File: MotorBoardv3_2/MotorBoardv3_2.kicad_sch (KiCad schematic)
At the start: 79 parts, among them J1 Bump0, J11 GP2Y0A41SK0F, J12 GP2Y0A41SK0F, J13 GP2Y0A41SK0F, J15 7.2, J16 LP5.0, J17 ELA, J18 ERA, J19 Voltage Display, J2 Bump1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

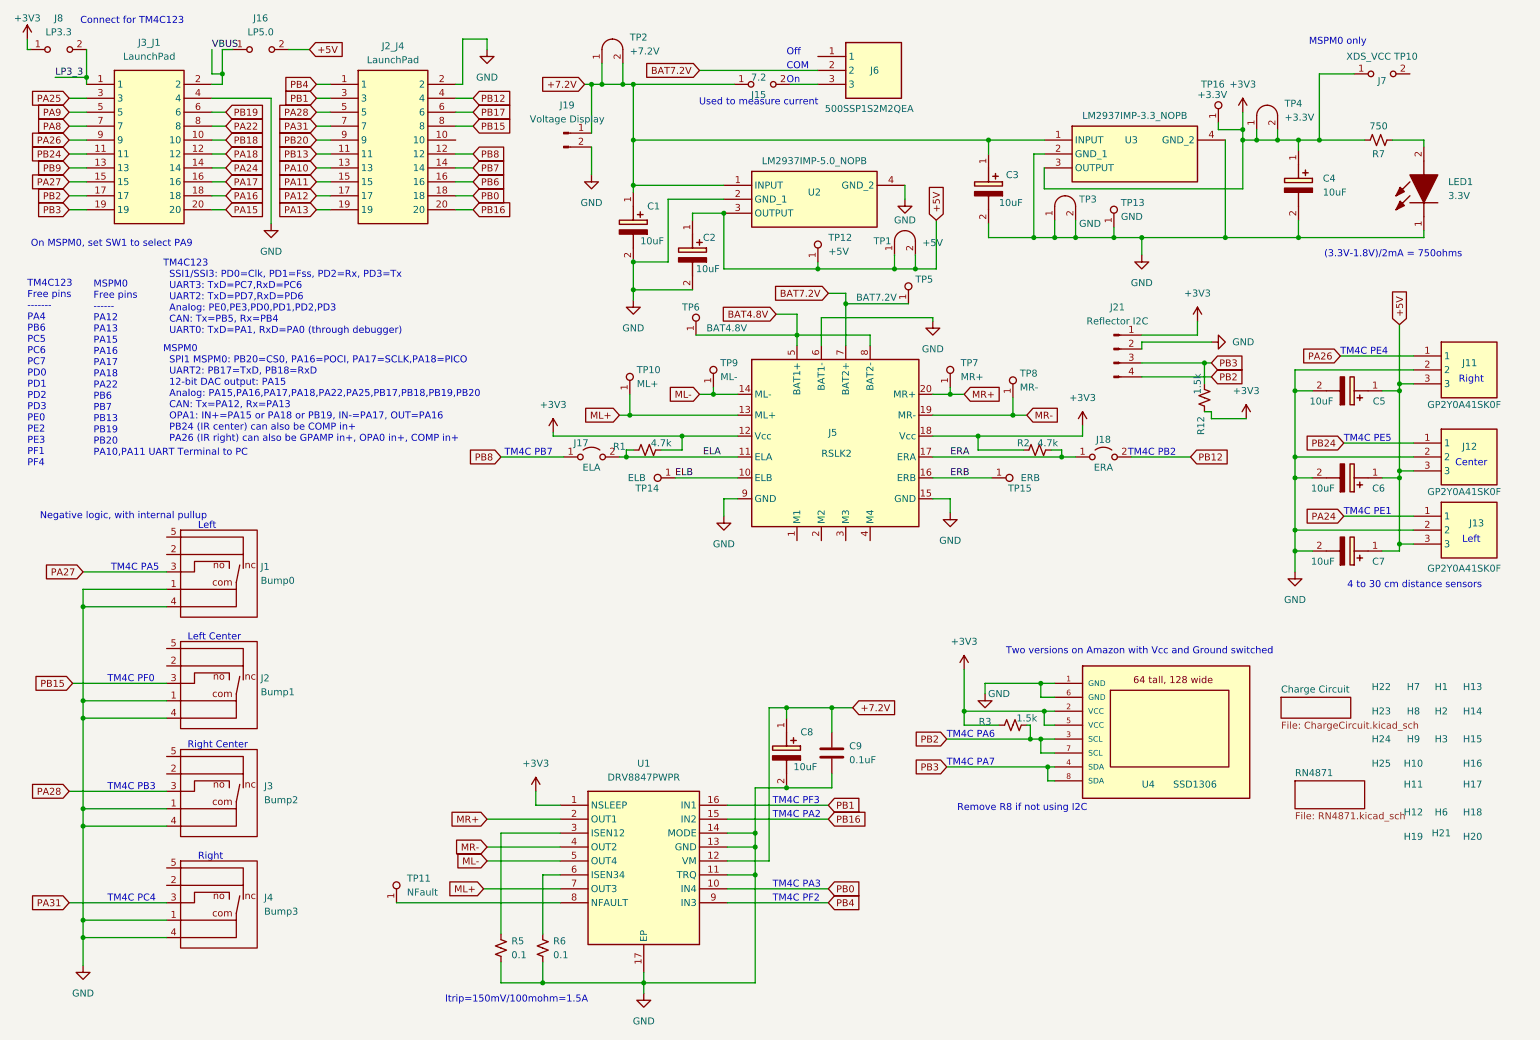
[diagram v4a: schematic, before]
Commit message: Added voltage display
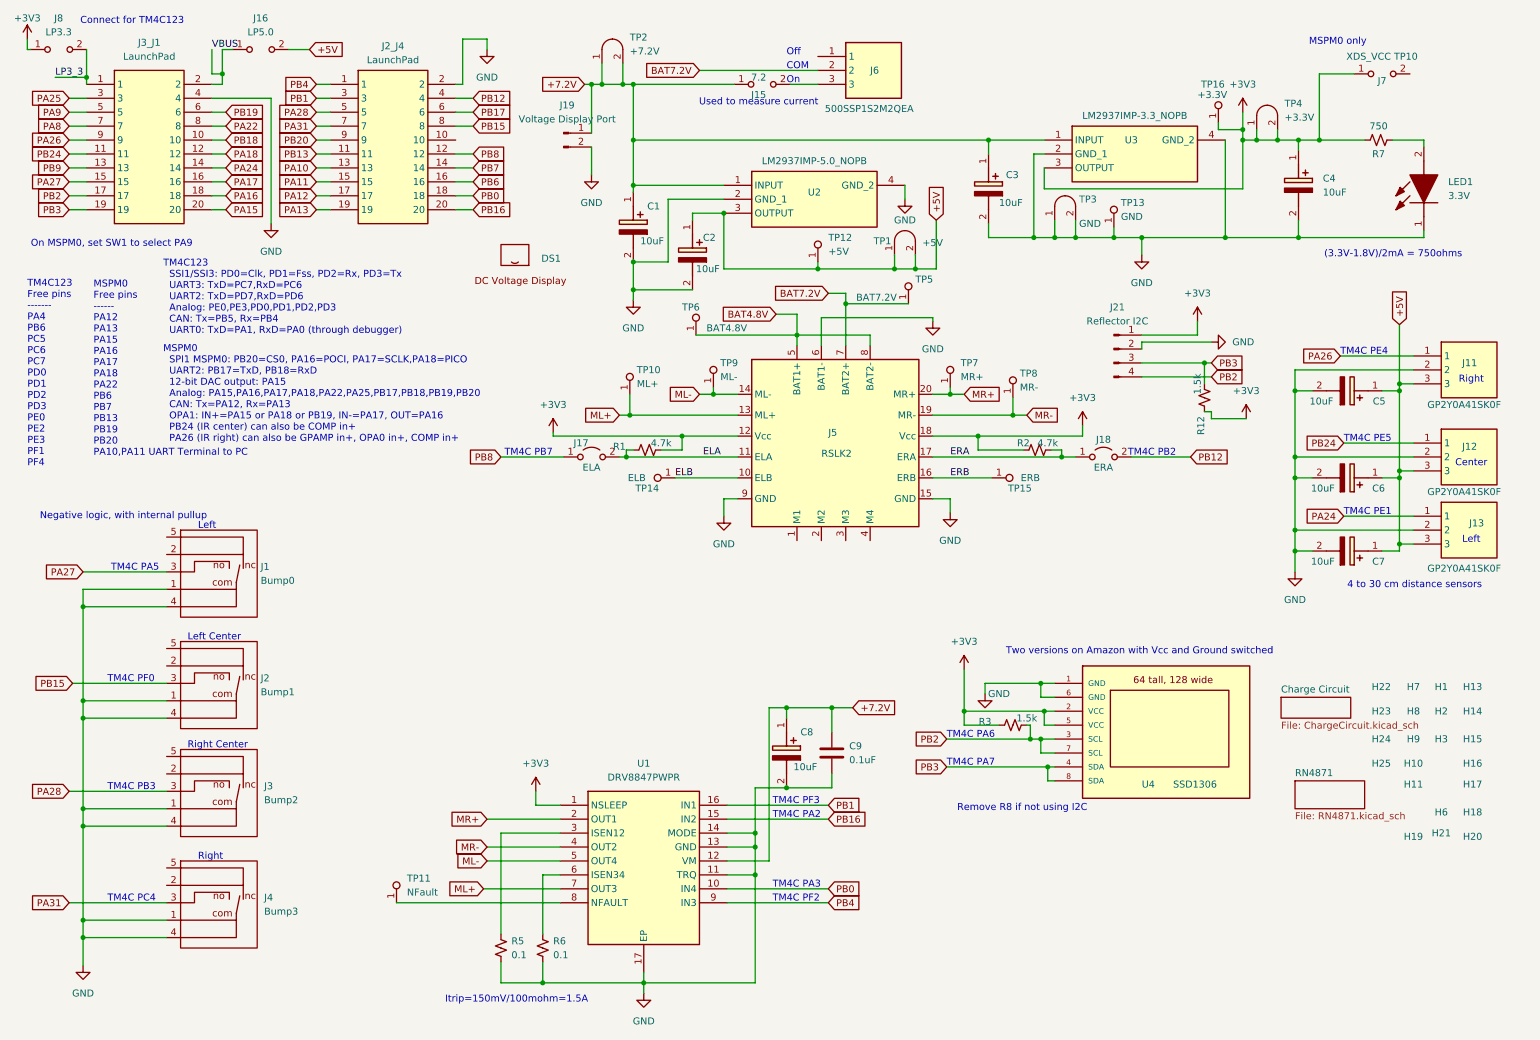
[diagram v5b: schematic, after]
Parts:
- removed H12: ~, RSLK2:MountingHole_4_40, symbol RSLK2:MountingHole
- added DS1: ~, VoltageDisplay:PRT-14313, symbol VoltageDisplay:VoltageDisplay
- J19: value Voltage Display -> Voltage Display Port
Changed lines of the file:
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@@
 	)
 	(symbol
-		(lib_id "RSLK2:MountingHole")
-		(at 271.78 160.655 0)
-		(unit 1)
-		(exclude_from_sim no)
-		(in_bom yes)
-		(on_board yes)
-		(dnp no)
-		(fields_autoplaced yes)
-		(property "Reference" "H12"
-			(at 267.97 158.115 0)
-			(effects
-				(font
-					(size 1.27 1.27)
-				)
-			)
-		)
-		(property "Value" "~"
-			(at 271.78 160.655 0)
-			(effects
-				(font
-					(size 1.27 1.27)
-				)
-			)
-		)
-		(property "Footprint" "RSLK2:MountingHole_4_40"
-			(at 271.78 160.655 0)
-			(effects
-				(font
-					(size 1.27 1.27)
-				)
-				(hide yes)
-			)
-		)
-		(property "Datasheet" ""
-			(at 271.78 160.655 0)
-			(effects
-				(font
-					(size 1.27 1.27)
-				)
-				(hide yes)
-			)
-		)
-		(property "Description" "Drill hole for 4-40 screw"
-			(at 271.78 160.655 0)
-			(effects
-				(font
-					(size 1.27 1.27)
-				)
-				(hide yes)
-			)
-		)
-		(instances
-			(project "MotorBoardv3_2"
-				(path "/69b823fd-c065-40ff-9bb9-c5835555f3eb"
-					(reference "H12")
-					(unit 1)
-				)
-			)
-		)
-	)
-	(symbol
 		(lib_id "RSLK2:D2F-01L30-D3_5pin")
 		(at 45.72 137.795 0)
@@
 			)
 		)
-		(property "Value" "Voltage Display"
+		(property "Value" "Voltage Display Port"
 			(at 113.665 31.75 0)
 			(effects
@@
 					(unit 1)
 				)
+			)
+		)
+	)
+	(symbol
+		(lib_id "VoltageDisplay:VoltageDisplay")
+		(at 104.14 58.42 0)
+		(unit 1)
+		(exclude_from_sim no)
+		(in_bom yes)
+		(on_board yes)
+		(dnp no)
+		(property "Reference" "DS1"
+			(at 108.966 57.15 0)
+			(effects
+				(font
+					(size 1.27 1.27)
+				)
+				(justify left)
+			)
+		)
+		(property "Value" "~"
+			(at 115.57 59.6928 0)
+			(effects
+				(font
+					(size 1.27 1.27)
+				)
+				(justify left)
+			)
+		)
+		(property "Footprint" "VoltageDisplay:PRT-14313"
+			(at 104.14 58.42 0)
+			(effects
+				(font
+					(size 1.27 1.27)
+				)
+				(hide yes)
+			)
+		)
+		(property "Datasheet" ""
+			(at 104.14 58.42 0)
+			(effects
+				(font
+					(size 1.27 1.27)
+				)
+				(hide yes)
+			)
+		)
+		(property "Description" ""
+			(at 104.14 58.42 0)
+			(effects
+				(font
+					(size 1.27 1.27)
+				)
+				(hide yes)
+			)
+		)
+		(instances
+			(project ""
+				(path "/69b823fd-c065-40ff-9bb9-c5835555f3eb"
+					(reference "DS1")
+					(unit 1)
+				)
